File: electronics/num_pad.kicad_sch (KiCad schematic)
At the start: 18 parts, among them SW69 SW_SPST, SW70 SW_SPST, SW71 SW_SPST, SW72 SW_SPST, SW73 SW_SPST, SW74 SW_SPST, SW75 SW_SPST, SW76 SW_SPST, SW77 SW_SPST, SW78 SW_SPST, SW79 SW_SPST, SW80 SW_SPST, SW81 SW_SPST, SW82 SW_SPST, SW83 SW_SPST, SW84 SW_SPST, SW85 SW_SPST, U5 MAX7314AEG+

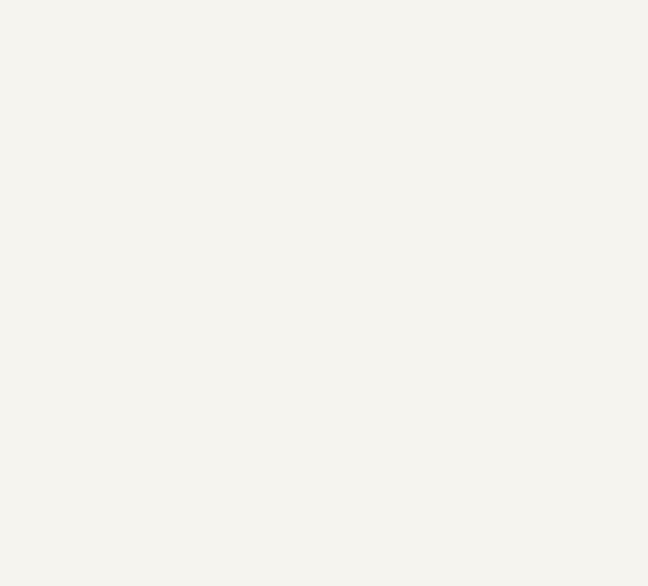
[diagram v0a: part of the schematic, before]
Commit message: add i2c headers to schematic
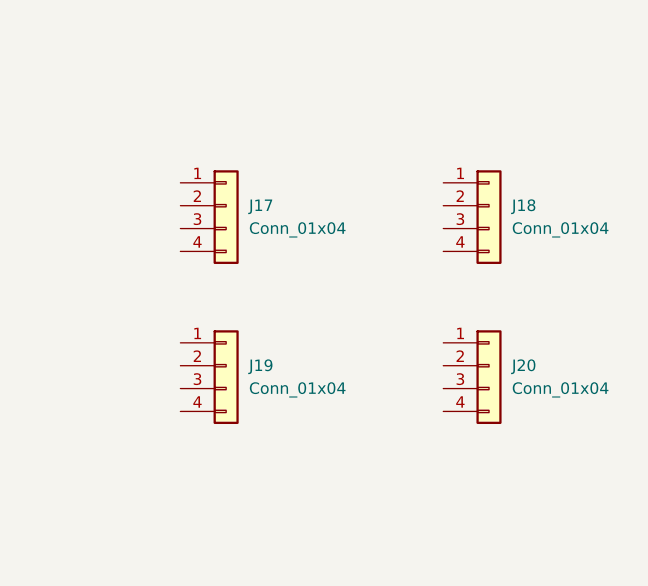
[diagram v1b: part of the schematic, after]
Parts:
- added J17, J18, J19, J20: Conn_01x04, symbol Connector_Generic:Conn_01x04
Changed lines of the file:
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@@
     (pin "2")
+  )
+  (symbol (lib_id "Connector_Generic:Conn_01x04") (at 187.96 86.36 0) (unit 1)
+    (in_bom yes) (on_board yes) (fields_autoplaced)
+    (property "Reference" "J19" (id 0) (at 190.5 86.3599 0)
+      (effects (font (size 1.27 1.27)) (justify left))
+    )
+    (property "Value" "Conn_01x04" (id 1) (at 190.5 88.8999 0)
+      (effects (font (size 1.27 1.27)) (justify left))
+    )
+    (property "Footprint" "" (id 2) (at 187.96 86.36 0)
+      (effects (font (size 1.27 1.27)) hide)
+    )
+    (property "Datasheet" "~" (id 3) (at 187.96 86.36 0)
+      (effects (font (size 1.27 1.27)) hide)
+    )
+    (pin "1")
+    (pin "2")
+    (pin "3")
+    (pin "4")
   )
   (symbol (lib_name "SW_SPST_8") (lib_id "Kailh:SW_SPST") (at 43.18 107.95 0) (unit 1)
@@
     (pin "9")
   )
+  (symbol (lib_id "Connector_Generic:Conn_01x04") (at 217.17 86.36 0) (unit 1)
+    (in_bom yes) (on_board yes) (fields_autoplaced)
+    (property "Reference" "J20" (id 0) (at 219.71 86.3599 0)
+      (effects (font (size 1.27 1.27)) (justify left))
+    )
+    (property "Value" "Conn_01x04" (id 1) (at 219.71 88.8999 0)
+      (effects (font (size 1.27 1.27)) (justify left))
+    )
+    (property "Footprint" "" (id 2) (at 217.17 86.36 0)
+      (effects (font (size 1.27 1.27)) hide)
+    )
+    (property "Datasheet" "~" (id 3) (at 217.17 86.36 0)
+      (effects (font (size 1.27 1.27)) hide)
+    )
+    (pin "1")
+    (pin "2")
+    (pin "3")
+    (pin "4")
+  )
+  (symbol (lib_id "Connector_Generic:Conn_01x04") (at 217.17 68.58 0) (unit 1)
+    (in_bom yes) (on_board yes) (fields_autoplaced)
+    (property "Reference" "J18" (id 0) (at 219.71 68.5799 0)
+      (effects (font (size 1.27 1.27)) (justify left))
+    )
+    (property "Value" "Conn_01x04" (id 1) (at 219.71 71.1199 0)
+      (effects (font (size 1.27 1.27)) (justify left))
+    )
+    (property "Footprint" "" (id 2) (at 217.17 68.58 0)
+      (effects (font (size 1.27 1.27)) hide)
+    )
+    (property "Datasheet" "~" (id 3) (at 217.17 68.58 0)
+      (effects (font (size 1.27 1.27)) hide)
+    )
+    (pin "1")
+    (pin "2")
+    (pin "3")
+    (pin "4")
+  )
   (symbol (lib_name "SW_SPST_11") (lib_id "Kailh:SW_SPST") (at 83.82 107.95 0) (unit 1)
     (in_bom yes) (on_board yes) (fields_autoplaced)
@@
     (pin "2")
   )
+  (symbol (lib_id "Connector_Generic:Conn_01x04") (at 187.96 68.58 0) (unit 1)
+    (in_bom yes) (on_board yes) (fields_autoplaced)
+    (property "Reference" "J17" (id 0) (at 190.5 68.5799 0)
+      (effects (font (size 1.27 1.27)) (justify left))
+    )
+    (property "Value" "Conn_01x04" (id 1) (at 190.5 71.1199 0)
+      (effects (font (size 1.27 1.27)) (justify left))
+    )
+    (property "Footprint" "" (id 2) (at 187.96 68.58 0)
+      (effects (font (size 1.27 1.27)) hide)
+    )
+    (property "Datasheet" "~" (id 3) (at 187.96 68.58 0)
+      (effects (font (size 1.27 1.27)) hide)
+    )
+    (pin "1")
+    (pin "2")
+    (pin "3")
+    (pin "4")
+  )
   (symbol (lib_name "SW_SPST_5") (lib_id "Kailh:SW_SPST") (at 43.18 156.21 0) (unit 1)

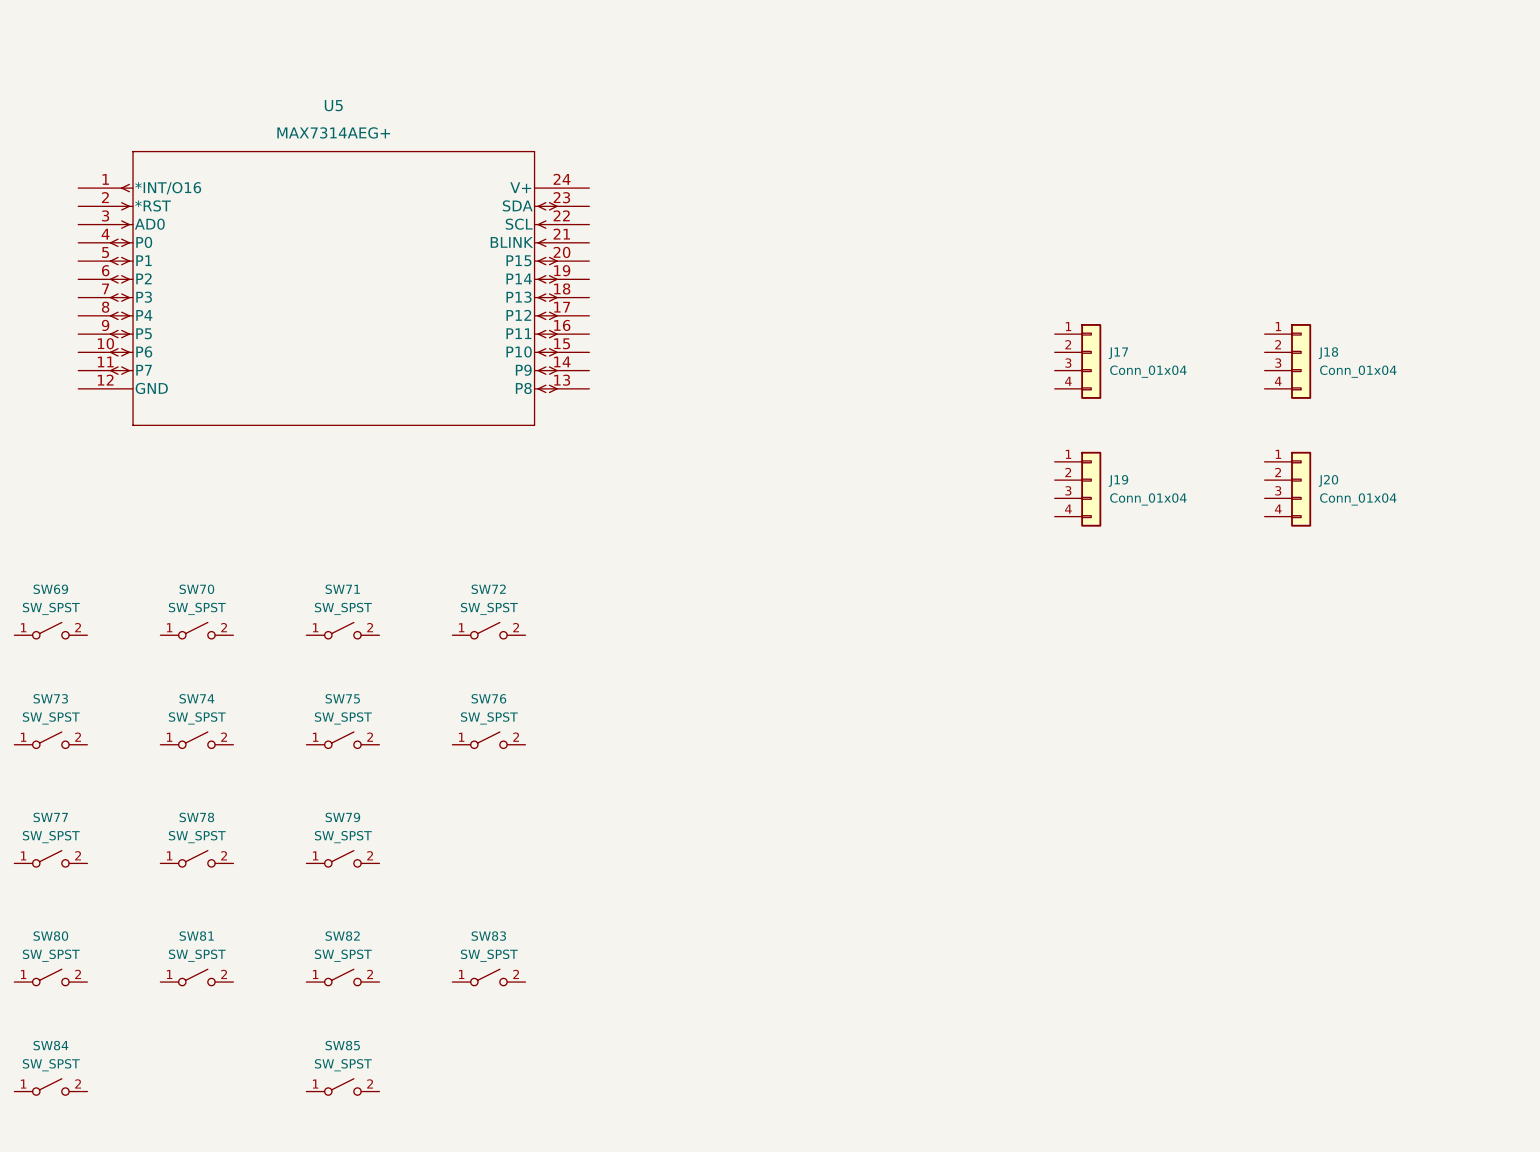
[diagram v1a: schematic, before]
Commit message: label switch nets
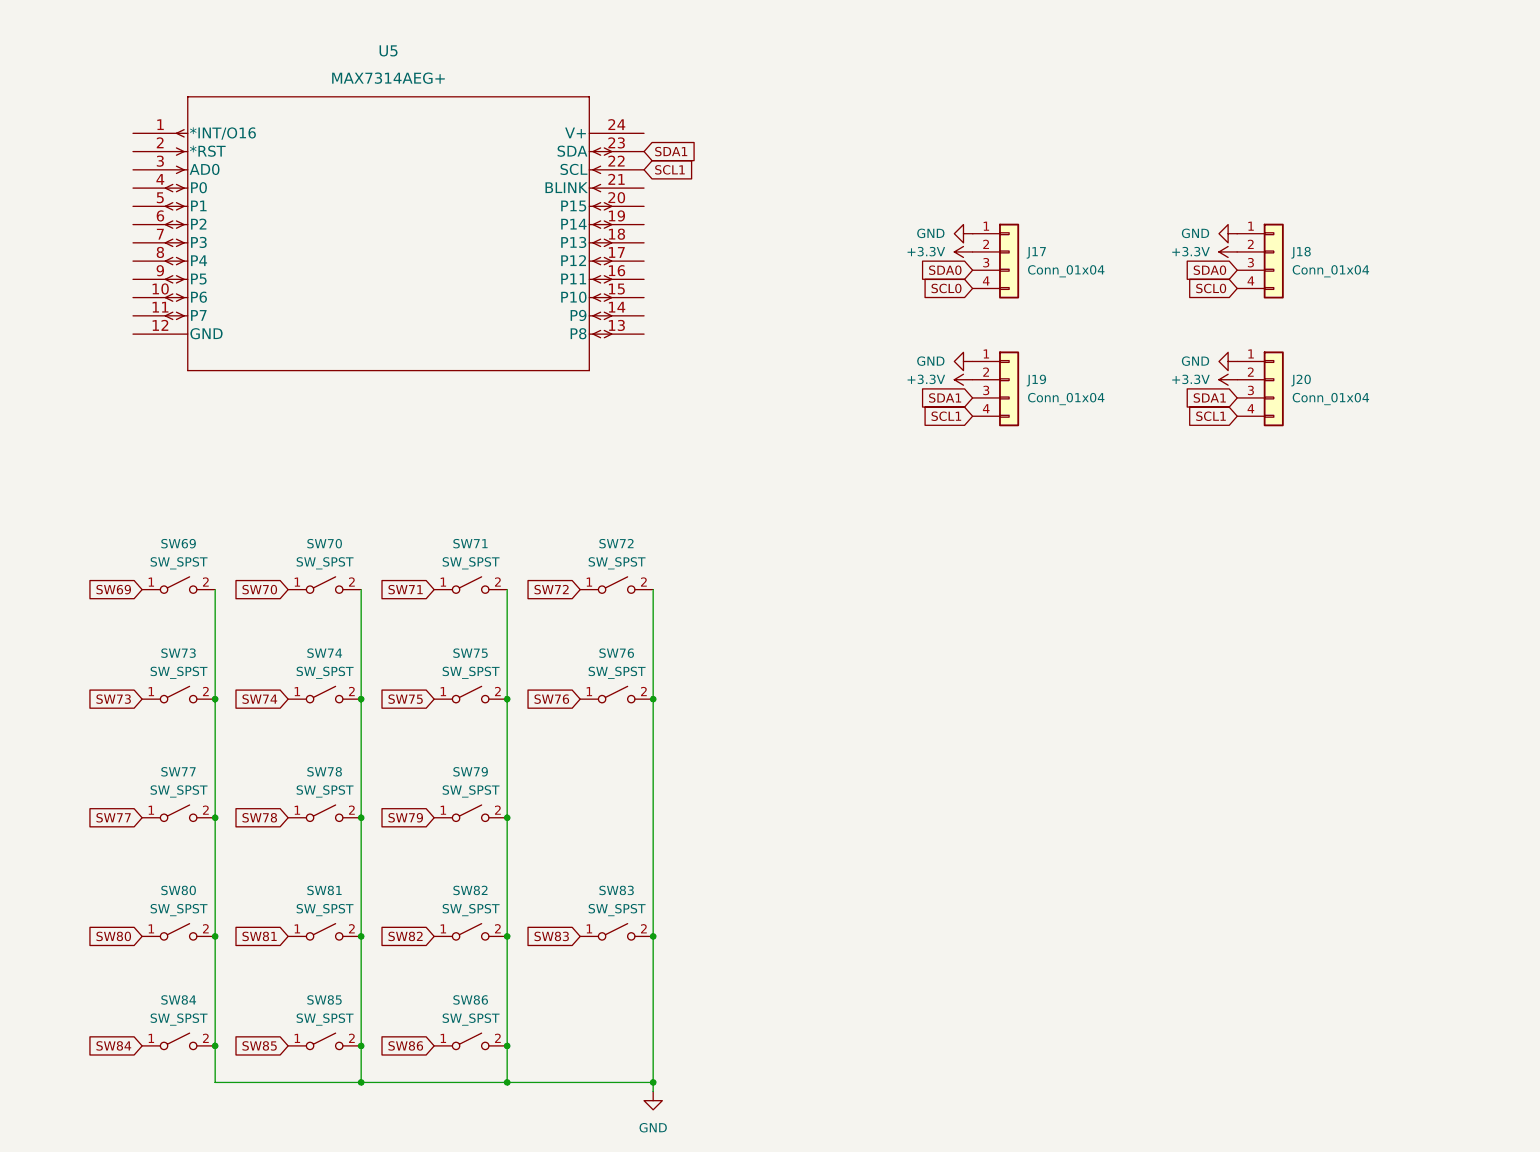
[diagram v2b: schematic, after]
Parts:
- added SW86: SW_SPST, Kailh:Kailh_socket_MX, symbol Kailh:SW_SPST
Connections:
- net SW82: now reaches SW82.1 (A)
- net GND: now reaches SW82.2 (B)
- net GND: now also J17.1 (Pin_1), J18.1 (Pin_1), J19.1 (Pin_1), J20.1 (Pin_1), SW69.2 (B), SW70.2 (B), SW71.2 (B), SW72.2 (B), SW73.2 (B), SW74.2 (B), SW75.2 (B), SW76.2 (B), SW77.2 (B), SW78.2 (B), SW79.2 (B), SW80.2 (B), SW81.2 (B), SW83.2 (B), SW84.2 (B), SW85.2 (B), SW86.2 (B)
- net SW74: now reaches SW74.1 (A)
- net SW78: now reaches SW78.1 (A)
- net SW75: now reaches SW75.1 (A)
- net SW77: now reaches SW77.1 (A)
- net SW84: now reaches SW84.1 (A)
- net SW70: now reaches SW70.1 (A)
- net +3V3: now reaches J19.2 (Pin_2)
- net +3V3: now also J17.2 (Pin_2), J18.2 (Pin_2), J20.2 (Pin_2)
- net SDA1: now reaches J19.3 (Pin_3)
- net SDA1: now also J20.3 (Pin_3), U5.23 (SDA)
- net SCL1: now reaches J19.4 (Pin_4)
- net SCL1: now also J20.4 (Pin_4), U5.22 (SCL)
- net SW69: now reaches SW69.1 (A)
- net SW79: now reaches SW79.1 (A)
- net SW76: now reaches SW76.1 (A)
- net SW72: now reaches SW72.1 (A)
- net SW83: now reaches SW83.1 (A)
- net SW73: now reaches SW73.1 (A)
- net SW81: now reaches SW81.1 (A)
- net SW85: now reaches SW85.1 (A)
- net SDA0: now reaches J18.3 (Pin_3)
- net SDA0: now also J17.3 (Pin_3)
- net SCL0: now reaches J18.4 (Pin_4)
- net SCL0: now also J17.4 (Pin_4)
- net SW71: now reaches SW71.1 (A)
- net SW80: now reaches SW80.1 (A)
- new net SW86: SW86.1 (A)

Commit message: fix numberpad switches
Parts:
- removed SW86: SW_SPST, Kailh:Kailh_socket_MX, symbol Kailh:SW_SPST
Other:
- moved on the sheet: SW85
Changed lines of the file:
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@@
     (company "OSHMount Tech")
   )
+  (junction (at 86.36 170.18) (diameter 0) (color 0 0 0 0)
+  )
+  (junction (at 106.68 133.35) (diameter 0) (color 0 0 0 0)
+  )
+  (junction (at 66.04 165.1) (diameter 0) (color 0 0 0 0)
+  )
+  (junction (at 66.04 116.84) (diameter 0) (color 0 0 0 0)
+  )
+  (junction (at 106.68 116.84) (diameter 0) (color 0 0 0 0)
+  )
+  (junction (at 127 116.84) (diameter 0) (color 0 0 0 0)
+  )
+  (junction (at 127 149.86) (diameter 0) (color 0 0 0 0)
+  )
+  (junction (at 86.36 149.86) (diameter 0) (color 0 0 0 0)
+  )
+  (junction (at 127 170.18) (diameter 0) (color 0 0 0 0)
+  )
+  (junction (at 66.04 149.86) (diameter 0) (color 0 0 0 0)
+  )
+  (junction (at 66.04 133.35) (diameter 0) (color 0 0 0 0)
+  )
   (junction (at 106.68 165.1) (diameter 0) (color 0 0 0 0)
   )
-  (junction (at 86.36 170.18) (diameter 0) (color 0 0 0 0)
-  )
-  (junction (at 86.36 165.1) (diameter 0) (color 0 0 0 0)
-  )
-  (junction (at 106.68 133.35) (diameter 0) (color 0 0 0 0)
-  )
-  (junction (at 66.04 165.1) (diameter 0) (color 0 0 0 0)
-  )
-  (junction (at 66.04 116.84) (diameter 0) (color 0 0 0 0)
-  )
-  (junction (at 106.68 116.84) (diameter 0) (color 0 0 0 0)
-  )
-  (junction (at 127 116.84) (diameter 0) (color 0 0 0 0)
-  )
-  (junction (at 127 149.86) (diameter 0) (color 0 0 0 0)
-  )
-  (junction (at 86.36 149.86) (diameter 0) (color 0 0 0 0)
-  )
-  (junction (at 127 170.18) (diameter 0) (color 0 0 0 0)
-  )
-  (junction (at 66.04 149.86) (diameter 0) (color 0 0 0 0)
-  )
-  (junction (at 66.04 133.35) (diameter 0) (color 0 0 0 0)
-  )
   (junction (at 106.68 149.86) (diameter 0) (color 0 0 0 0)
   )
@@
     (stroke (width 0) (type default) (color 0 0 0 0))
   )
-  (wire (pts (xy 86.36 149.86) (xy 86.36 165.1))
+  (wire (pts (xy 86.36 149.86) (xy 86.36 170.18))
     (stroke (width 0) (type default) (color 0 0 0 0))
   )
@@
     (stroke (width 0) (type default) (color 0 0 0 0))
   )
-  (wire (pts (xy 86.36 165.1) (xy 86.36 170.18))
+  (wire (pts (xy 106.68 165.1) (xy 106.68 170.18))
     (stroke (width 0) (type default) (color 0 0 0 0))
   )
@@
     (stroke (width 0) (type default) (color 0 0 0 0))
   )
-  (wire (pts (xy 106.68 165.1) (xy 106.68 170.18))
-    (stroke (width 0) (type default) (color 0 0 0 0))
-  )
   (wire (pts (xy 66.04 101.6) (xy 66.04 116.84))
     (stroke (width 0) (type default) (color 0 0 0 0))
@@
     )
   )
-  (global_label "SW85" (shape input) (at 76.2 165.1 180) (fields_autoplaced)
-    (effects (font (size 1.27 1.27)) (justify right))
-    (property "Intersheet References" "${INTERSHEET_REFS}" (id 0) (at 68.7069 165.0206 0)
+  (global_label "SW85" (shape input) (at 96.52 165.1 180) (fields_autoplaced)
+    (effects (font (size 1.27 1.27)) (justify right))
+    (property "Intersheet References" "${INTERSHEET_REFS}" (id 0) (at 89.0269 165.0206 0)
       (effects (font (size 1.27 1.27)) (justify right) hide)
     )
@@
     (effects (font (size 1.27 1.27)) (justify right))
     (property "Intersheet References" "${INTERSHEET_REFS}" (id 0) (at 109.3469 116.7606 0)
-      (effects (font (size 1.27 1.27)) (justify right) hide)
-    )
-  )
-  (global_label "SW86" (shape input) (at 96.52 165.1 180) (fields_autoplaced)
-    (effects (font (size 1.27 1.27)) (justify right))
-    (property "Intersheet References" "${INTERSHEET_REFS}" (id 0) (at 89.0269 165.0206 0)
       (effects (font (size 1.27 1.27)) (justify right) hide)
     )
@@
     (pin "2")
   )
-  (symbol (lib_name "SW_SPST_9") (lib_id "Kailh:SW_SPST") (at 81.28 165.1 0) (unit 1)
-    (in_bom yes) (on_board yes) (fields_autoplaced)
-    (property "Reference" "SW85" (id 0) (at 81.28 158.75 0))
-    (property "Value" "SW_SPST" (id 1) (at 81.28 161.29 0))
-    (property "Footprint" "Kailh:Kailh_socket_MX" (id 2) (at 81.28 165.1 0)
-      (effects (font (size 1.27 1.27)) hide)
-    )
-    (property "Datasheet" "${OSHMOUNT_LIBRARY}/Kailh/Kailh_Polia_datasheet.pdf" (id 3) (at 81.28 165.1 0)
+  (symbol (lib_name "SW_SPST_9") (lib_id "Kailh:SW_SPST") (at 101.6 165.1 0) (unit 1)
+    (in_bom yes) (on_board yes) (fields_autoplaced)
+    (property "Reference" "SW85" (id 0) (at 101.6 158.75 0))
+    (property "Value" "SW_SPST" (id 1) (at 101.6 161.29 0))
+    (property "Footprint" "Kailh:Kailh_socket_MX" (id 2) (at 101.6 165.1 0)
+      (effects (font (size 1.27 1.27)) hide)
+    )
+    (property "Datasheet" "${OSHMOUNT_LIBRARY}/Kailh/Kailh_Polia_datasheet.pdf" (id 3) (at 101.6 165.1 0)
       (effects (font (size 1.27 1.27)) hide)
     )
@@
       (effects (font (size 1.27 1.27)) hide)
     )
-    (pin "1")
-    (pin "2")
-  )
-  (symbol (lib_name "SW_SPST_8") (lib_id "Kailh:SW_SPST") (at 101.6 165.1 0) (unit 1)
-    (in_bom yes) (on_board yes) (fields_autoplaced)
-    (property "Reference" "SW86" (id 0) (at 101.6 158.75 0))
-    (property "Value" "SW_SPST" (id 1) (at 101.6 161.29 0))
-    (property "Footprint" "Kailh:Kailh_socket_MX" (id 2) (at 101.6 165.1 0)
-      (effects (font (size 1.27 1.27)) hide)
-    )
-    (property "Datasheet" "${OSHMOUNT_LIBRARY}/Kailh/Kailh_Polia_datasheet.pdf" (id 3) (at 101.6 165.1 0)
-      (effects (font (size 1.27 1.27)) hide)
-    )

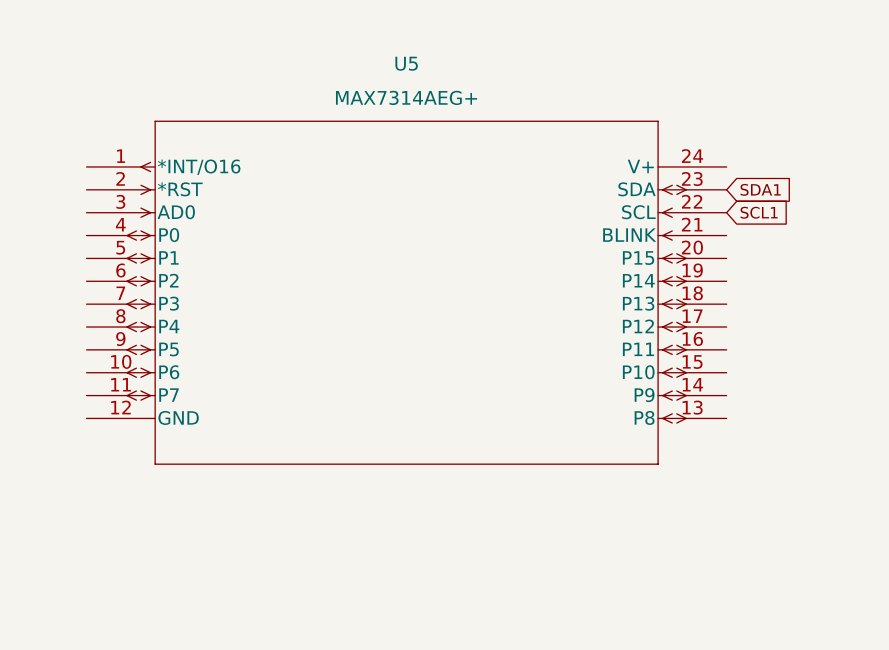
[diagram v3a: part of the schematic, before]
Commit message: change IO expander
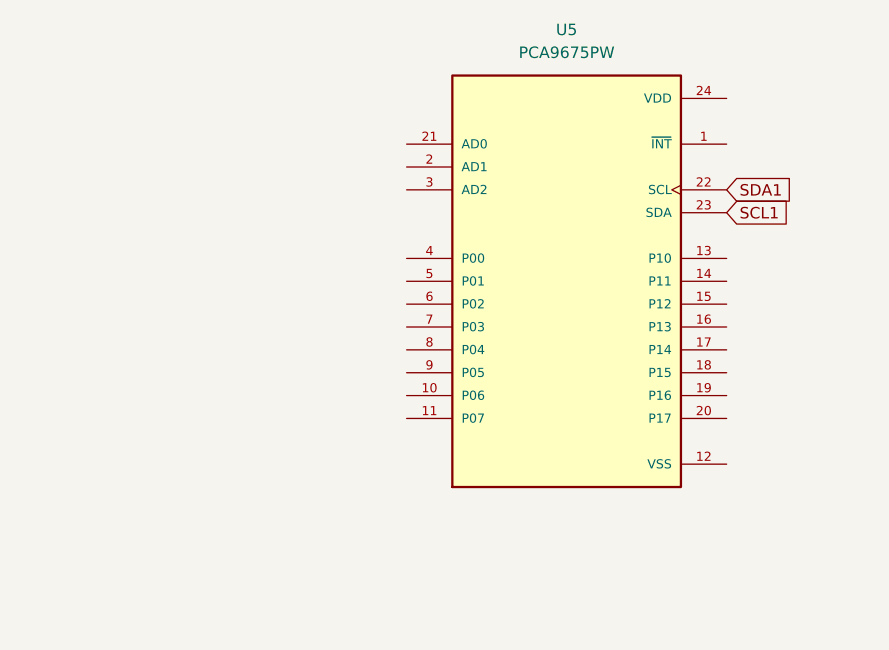
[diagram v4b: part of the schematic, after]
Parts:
- removed U5: MAX7314AEG+, MAX7314AEG:MAX7314AEG&plus_, symbol MAX7314AEG:MAX7314AEG+
- added U5: PCA9675PW, PCA9675PW:SOP65P640X110-24N, symbol PCA9675PW_118:PCA9675PW
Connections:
- net SCL1: now also U5.23 (SDA)
- net SDA1: now also U5.22 (SCL)
